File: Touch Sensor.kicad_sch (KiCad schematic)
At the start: 12 parts, among them J1 Conn_01x02_Pin, J2 Conn_01x04_Pin, U1 LMC555xN, U2 SN74LVC1G14DBV

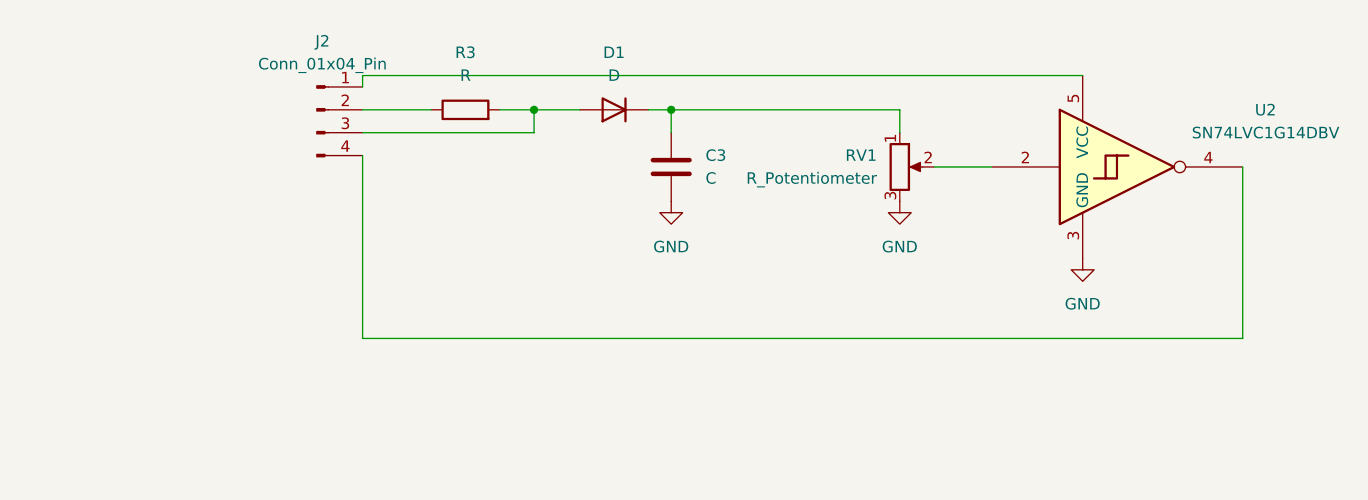
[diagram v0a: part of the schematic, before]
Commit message: modified touch circuit
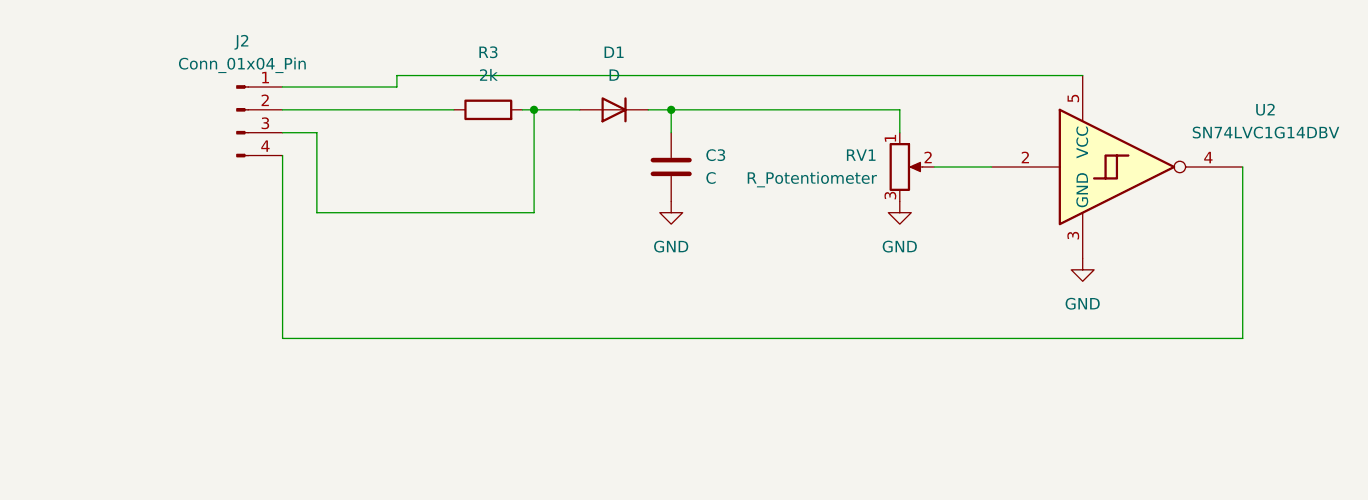
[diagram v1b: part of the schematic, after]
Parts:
- R3: value R -> 2k
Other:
- moved on the sheet: J2, R3
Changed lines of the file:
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@@
 	(wire
 		(pts
-			(xy 146.05 50.8) (xy 146.05 30.48)
-		)
-		(stroke
-			(width 0)
-			(type default)
-		)
-	)
-	(wire
-		(pts
-			(xy 146.05 21.59) (xy 226.06 21.59)
+			(xy 226.06 21.59) (xy 149.86 21.59)
 		)
 		(stroke
@@
 	(wire
 		(pts
-			(xy 161.29 25.4) (xy 165.1 25.4)
-		)
-		(stroke
-			(width 0)
-			(type default)
-		)
-	)
-	(wire
-		(pts
-			(xy 146.05 22.86) (xy 146.05 21.59)
+			(xy 163.83 25.4) (xy 165.1 25.4)
 		)
 		(stroke
@@
 	(wire
 		(pts
+			(xy 165.1 36.83) (xy 140.97 36.83)
+		)
+		(stroke
+			(width 0)
+			(type default)
+		)
+	)
+	(wire
+		(pts
 			(xy 22.86 76.2) (xy 39.37 76.2)
 		)
@@
 	(wire
 		(pts
-			(xy 165.1 27.94) (xy 165.1 25.4)
+			(xy 165.1 25.4) (xy 165.1 36.83)
 		)
 		(stroke
@@
 	(wire
 		(pts
-			(xy 146.05 25.4) (xy 153.67 25.4)
+			(xy 137.16 25.4) (xy 156.21 25.4)
 		)
 		(stroke
@@
 	(wire
 		(pts
-			(xy 146.05 27.94) (xy 165.1 27.94)
+			(xy 137.16 22.86) (xy 149.86 22.86)
 		)
 		(stroke
@@
 	(wire
 		(pts
-			(xy 243.84 50.8) (xy 146.05 50.8)
-		)
-		(stroke
-			(width 0)
-			(type default)
-		)
-	)
-	(wire
-		(pts
 			(xy 92.71 54.61) (xy 77.47 54.61)
 		)
@@
 	(wire
 		(pts
+			(xy 137.16 50.8) (xy 243.84 50.8)
+		)
+		(stroke
+			(width 0)
+			(type default)
+		)
+	)
+	(wire
+		(pts
 			(xy 80.01 72.39) (xy 60.96 72.39)
 		)
@@
 	(wire
 		(pts
+			(xy 137.16 30.48) (xy 137.16 50.8)
+		)
+		(stroke
+			(width 0)
+			(type default)
+		)
+	)
+	(wire
+		(pts
 			(xy 48.26 67.31) (xy 48.26 76.2)
 		)
@@
 	(wire
 		(pts
+			(xy 140.97 36.83) (xy 140.97 27.94)
+		)
+		(stroke
+			(width 0)
+			(type default)
+		)
+	)
+	(wire
+		(pts
 			(xy 69.85 44.45) (xy 22.86 44.45)
 		)
@@
 	(wire
 		(pts
+			(xy 149.86 21.59) (xy 149.86 22.86)
+		)
+		(stroke
+			(width 0)
+			(type default)
+		)
+	)
+	(wire
+		(pts
 			(xy 80.01 67.31) (xy 48.26 67.31)
 		)
@@
 		(pts
 			(xy 22.86 69.85) (xy 22.86 76.2)
+		)
+		(stroke
+			(width 0)
+			(type default)
+		)
+	)
+	(wire
+		(pts
+			(xy 140.97 27.94) (xy 137.16 27.94)
 		)
 		(stroke
@@
 	(symbol
 		(lib_id "Device:R")
-		(at 157.48 25.4 90)
+		(at 160.02 25.4 90)
 		(unit 1)
 		(exclude_from_sim no)
@@
 		(fields_autoplaced yes)
 		(property "Reference" "R3"
-			(at 157.48 19.05 90)
-			(effects
-				(font
-					(size 1.27 1.27)
-				)
-			)
-		)
-		(property "Value" "R"
-			(at 157.48 21.59 90)
+			(at 160.02 19.05 90)
+			(effects
+				(font
+					(size 1.27 1.27)
+				)
+			)
+		)
+		(property "Value" "2k"
+			(at 160.02 21.59 90)
 			(effects
 				(font
@@
 		)
 		(property "Footprint" ""
-			(at 157.48 27.178 90)
+			(at 160.02 27.178 90)
 			(effects
 				(font
@@
 		)
 		(property "Datasheet" "~"
-			(at 157.48 25.4 0)
+			(at 160.02 25.4 0)
 			(effects
 				(font
@@
 		)
 		(property "Description" "Resistor"
-			(at 157.48 25.4 0)
+			(at 160.02 25.4 0)
 			(effects
 				(font
@@
 	(symbol
 		(lib_id "Connector:Conn_01x04_Pin")
-		(at 140.97 25.4 0)
+		(at 132.08 25.4 0)
 		(unit 1)
 		(exclude_from_sim no)
@@
 		(fields_autoplaced yes)
 		(property "Reference" "J2"
-			(at 141.605 17.78 0)
+			(at 132.715 17.78 0)
 			(effects
 				(font
@@
 		)
 		(property "Value" "Conn_01x04_Pin"
-			(at 141.605 20.32 0)
+			(at 132.715 20.32 0)
 			(effects
 				(font
@@
 		)
 		(property "Footprint" "Connector_Wire:SolderWire-1.5sqmm_1x04_P6mm_D1.7mm_OD3mm"
-			(at 140.97 25.4 0)
+			(at 132.08 25.4 0)
 			(effects
 				(font
@@
 		)
 		(property "Datasheet" "~"
-			(at 140.97 25.4 0)
+			(at 132.08 25.4 0)
 			(effects
 				(font
@@
 		)
 		(property "Description" "Generic connector, single row, 01x04, script generated"
-			(at 140.97 25.4 0)
-			(effects
-				(font
+			(at 132.08 25.4 0)
+			(effects
+				(font
